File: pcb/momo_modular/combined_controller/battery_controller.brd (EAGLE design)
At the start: 50.5 x 32.8 mm, 38 parts, among them Q2 P-MOSFET, U1 XRP7659, U3 MCP1702, U4 PIC24F16KA101-X_PSSOP, U5 FLASH8MSOP8, U6 MCP73811

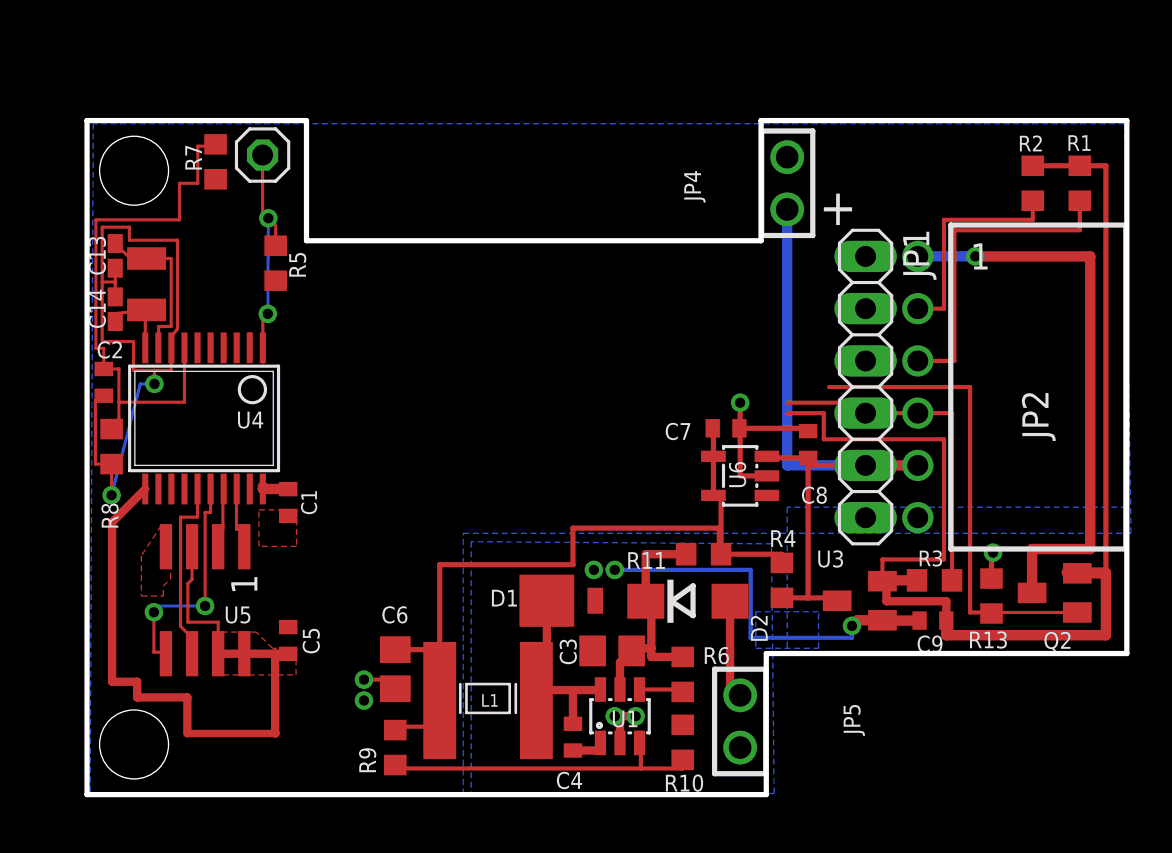
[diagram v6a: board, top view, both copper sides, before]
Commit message: Finish initial layout of revised controller board with enhanced pic
- now has battery backup of RTC
- new pic24 chip with 64K rom and 8K RAM
- lower power consumption
- removed current meter to battery for charging current (just measure
  the voltage over time)
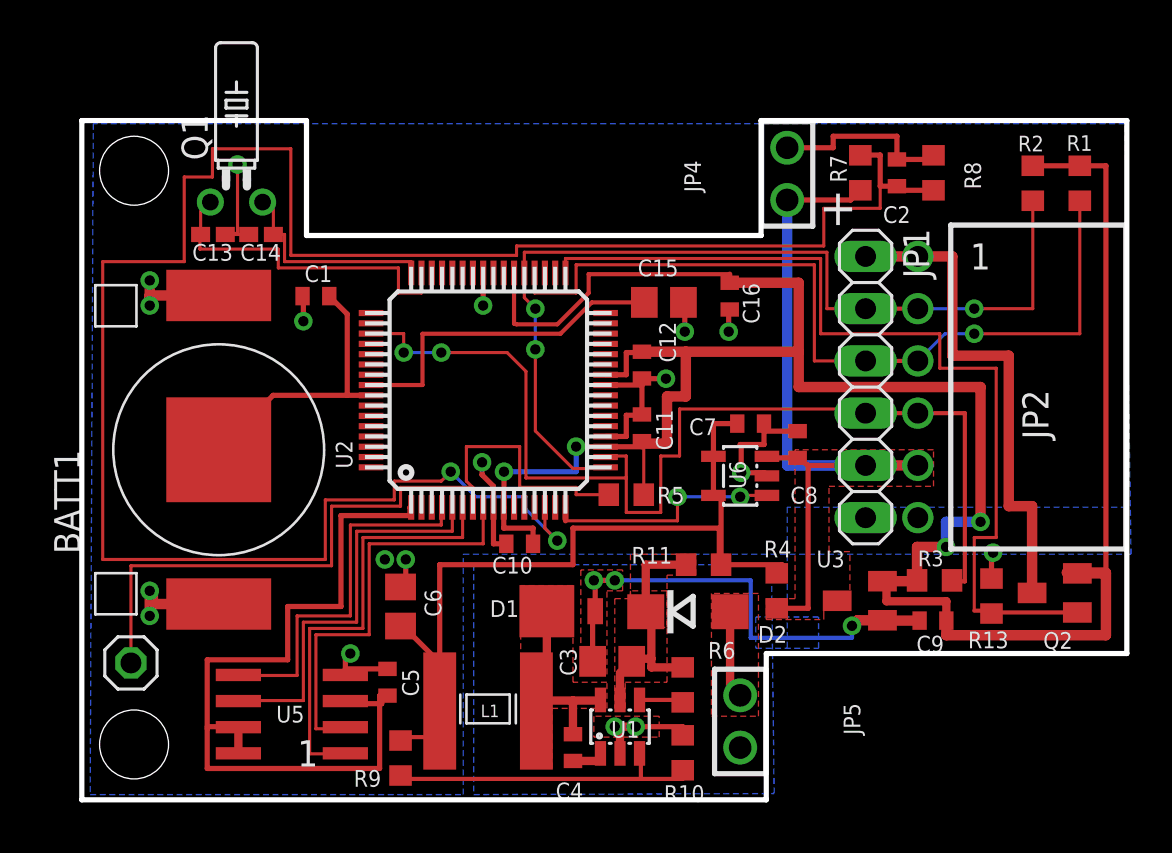
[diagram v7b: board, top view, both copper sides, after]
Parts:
- removed U4: PIC24F16KA101-X_PSSOP, components:SSOP20
- removed XT1: 32.768khz, components:1206
- added BATT1: CR1025-HOLDER, components:CR1025-HOLDER
- added C10, C11, C16: 100nF, rcl:C0402
- added C12: 100 nF, rcl:C0402
- added C15: 10 uF, rcl:C0805
- added Q1: (no value), crystal:TC26H
- added U2: PIC24FJ64GA306, components:TQFP64-10X10
- C1: value 100 nF -> 100nF
- moved R8 42.1 mm to (75.4, 42.4), turned to 270 degrees
- moved C2 39.9 mm to (73.7, 42.4), turned to 90 degrees
- moved R7 31.3 mm to (71.9, 42.4)
- moved JP3 25.5 mm to (36.4, 18.6)
- moved R5 20.4 mm to (60.5, 26.8), turned to 0 degrees
- moved C1 10.1 mm to (45.4, 36.4), turned to 180 degrees
- moved C14 7.96 mm to (42.7, 39.4), turned to 180 degrees
- moved U5 6.96 mm to (44.2, 16.1), turned to 90 degrees
- moved C5 5.24 mm to (48.9, 17.7)
- moved C13 4.86 mm to (40.4, 39.4), turned to 0 degrees
- moved C6 3.06 mm to (49.5, 21.3), turned to 90 degrees
- moved C7 1.22 mm to (66.5, 30.2)
- moved R4 0.57 mm to (67.8, 22.1)
- moved R9 0.57 mm to (49.5, 14.0)
- moved D1 0.51 mm to (56.6, 21.1)
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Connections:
- removed net N$15: JP3.1, R5.1, U4.1
- removed net N$24: C14.1, U4.10, XT1.P$2
- removed net N$25: C13.1, U4.9, XT1.P$1
- new net N$4: JP3.1, R5.1, U2.7
- new net N$6: C14.1, Q1.2, U2.48
- new net N$7: C13.1, Q1.1, U2.47
- new net VBAT: BATT1.+, C1.1, U2.57
- new net VCAP: C15.1, U2.56
- net CHG_EN: now also U2.16; no longer U4.14
- net CS: now also U2.6; no longer U4.18
- net GND: now also BATT1.-1, BATT1.-2, C10.2, C11.2, C12.2, C15.2, C16.2, U2.20, U2.25, U2.41, U2.9; no longer U4.19, U4.8
- net ICLK: now also U2.17, U2.37; no longer U4.12, U4.5
- net IDAT: now also U2.36; no longer U4.13
- net IRQ: now also U2.18, U2.51; no longer U4.4
- net MEM_POW: now also U2.1; no longer U4.11
- net SCLK: now also U2.5; no longer U4.15
- net SDI: now also U2.8; no longer U4.17
- net SDO: now also U2.4; no longer U4.16
- net VBAT_SAMP: now also U2.14; no longer U4.7
- net VCCINT: now also C10.1, C11.1, C12.1, C16.1, U2.10, U2.19, U2.26, U2.38; no longer C1.1, U4.20
- net VCC_EN: now also U2.33; no longer U4.2
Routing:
- net VBAT_SAMP: track 26.7 -> 101.3 mm, vias 0 -> 2
- net VCCINT: track 65.6 -> 122.7 mm, vias 0 -> 4
- net N$4: track 0.00 -> 37.5 mm
- net IRQ: track 16.6 -> 53.2 mm, vias 0 -> 2
- net ICLK: track 10.8 -> 45.8 mm, vias 0 -> 3
- net IDAT: track 15.7 -> 40.6 mm, vias 0 -> 1
- net VCC_EN: track 24.1 -> 45.0 mm
- net CS: track 3.45 -> 21.2 mm
- net SDI: track 3.30 -> 20.4 mm
- net N$7: track 0.00 -> 16.7 mm
- net GND: track 68.7 -> 85.2 mm, vias 11 -> 21
- net VCAP: track 0.00 -> 16.4 mm
- net VBAT: track 0.00 -> 13.7 mm
- net N$15: track 11.8 -> 0.00 mm, vias 2 -> 0
- net CHG_EN: track 0.00 -> 11.7 mm, vias 0 -> 2
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- added copper zone on layer 1, net +18V
- added copper zone on layer 1, net N$1
- added copper zone on layer 1, net N$13
- added copper zone on layer 1, net V+
- removed copper zone on layer 1, net MEM_POW
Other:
- board size 50.5 x 32.8 mm -> 50.8 x 33 mm

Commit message: Finish laying out combined_controller board
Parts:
- moved C10 1.08 mm to (54.3, 24.5)
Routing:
- net VCCINT: track 122.7 -> 119.9 mm
- net VBAT_SAMP: track 101.3 -> 99.3 mm
- net IRQ: track 53.2 -> 51.9 mm
- net N$4: track 37.5 -> 36.7 mm
- added copper zone on layer 1, net N$5
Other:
- board text added: "+ in center"
